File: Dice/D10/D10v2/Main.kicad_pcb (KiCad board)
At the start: 2 copper layers, 88.8 x 48.5 mm, 65 parts, among them J1 Conn_01x14, J2 Conn_01x04, J3 Conn_01x02, J4 DNP, P5 COILA, P6 COILB, U1 N52810_QFN32, U2 KXTJ3-1057, U3 PJ75AL50SA, U4 ME6215, U5 MCP73832T-2ACI/OT, U6 MT9700, U7 SN74LVC1G08, U8 TMR1366, Y1 32MHz 40ppm

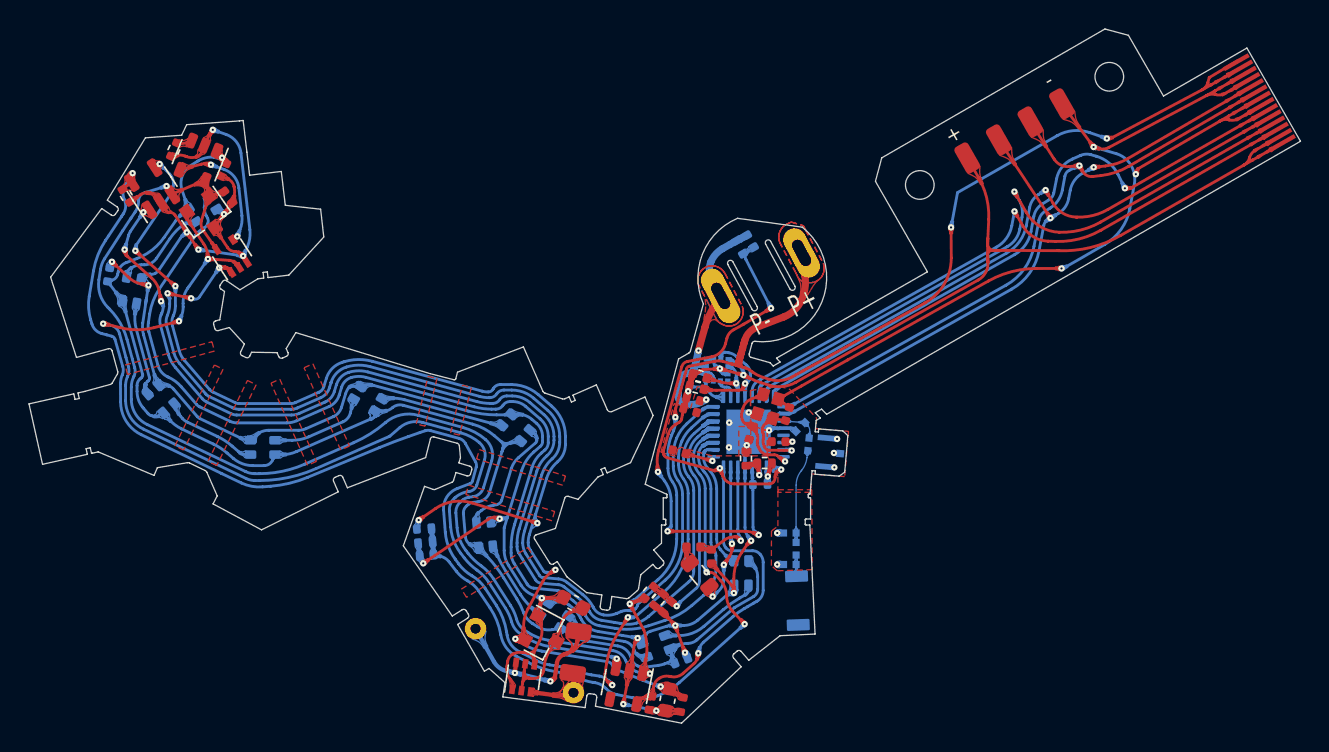
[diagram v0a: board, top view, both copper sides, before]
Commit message: Updated D6, D8, D10 boards
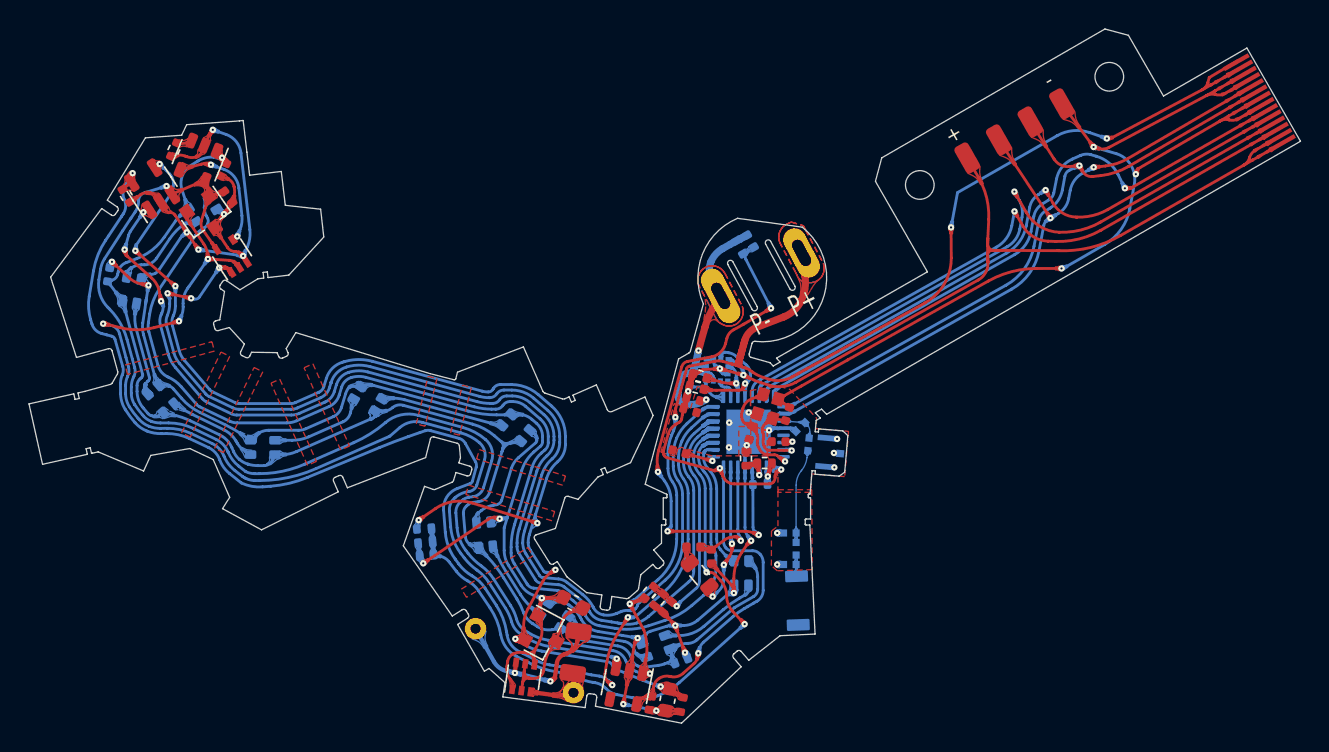
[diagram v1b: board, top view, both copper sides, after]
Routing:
- added copper zone on B.Cu, net Net-(D8-Pad3)
- added copper zone on B.Cu, net VDC
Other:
- outline, holes or cut-outs redrawn

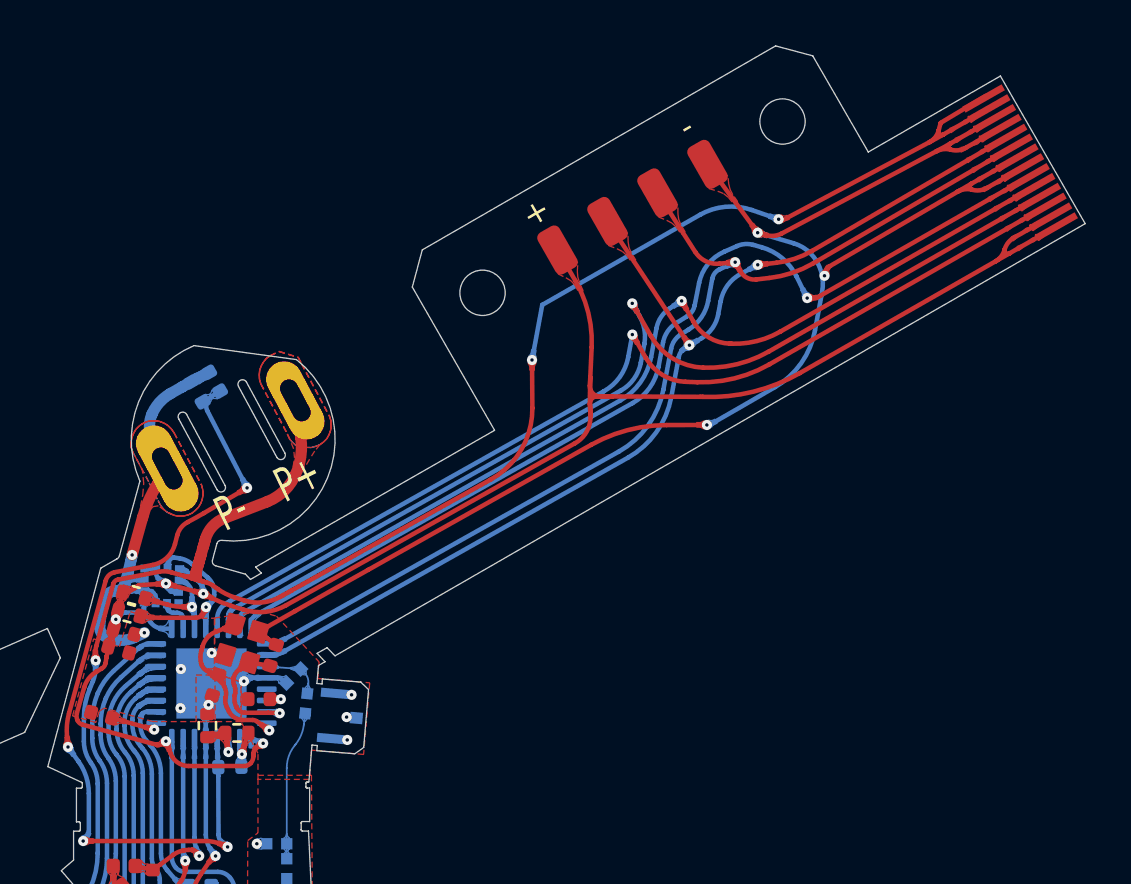
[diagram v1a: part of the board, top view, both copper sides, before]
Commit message: Updated all dice boards with smaller programming connector. Added ChargerV16
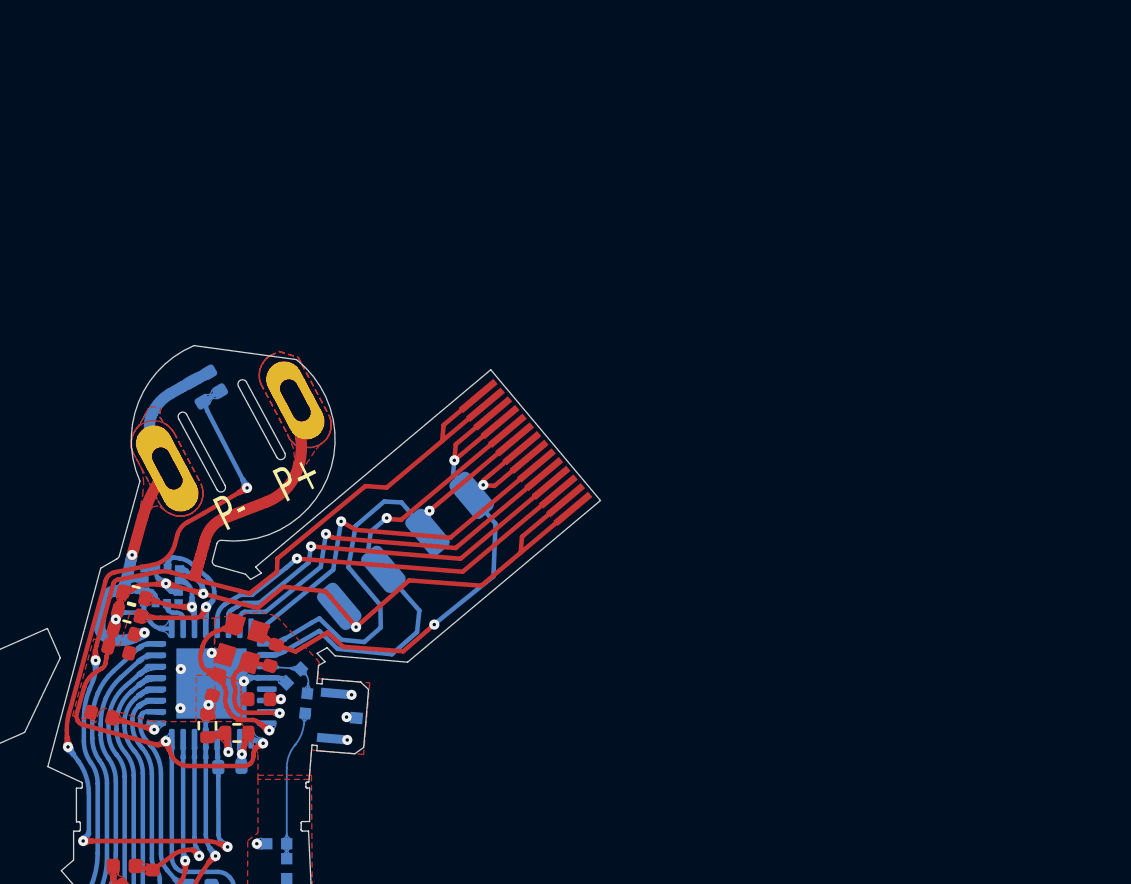
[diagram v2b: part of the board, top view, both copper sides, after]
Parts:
- J2: moved to B.Cu
- moved J1 25.9 mm to (162.8, 98.1), turned to -50 degrees
- moved J2 18.2 mm to (159.6, 105.0), turned to 40 degrees
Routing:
- net GND: track 258.1 -> 218.9 mm
- net VDD: track 107.6 -> 75.3 mm, vias 6 -> 7
- net +BATT: track 170.9 -> 140.9 mm, vias 6 -> 4
- net SWO: track 46.1 -> 17.5 mm
- net SWDIO: track 48.1 -> 20.7 mm, vias 2 -> 1
- net RESET: track 43.9 -> 16.6 mm
- net TXO: track 44.4 -> 17.9 mm
- net RXI: track 43.4 -> 17.2 mm
- net SWDCLK: track 47.1 -> 21.0 mm
- added copper zone on B.Cu, net Net-(C2-Pad2)
- added copper zone on B.Cu, net Net-(C3-Pad1)
- removed copper zone on F.Cu, net SWDCLK
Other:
- board size 88.8 x 48.5 mm -> 67.4 x 42.1 mm

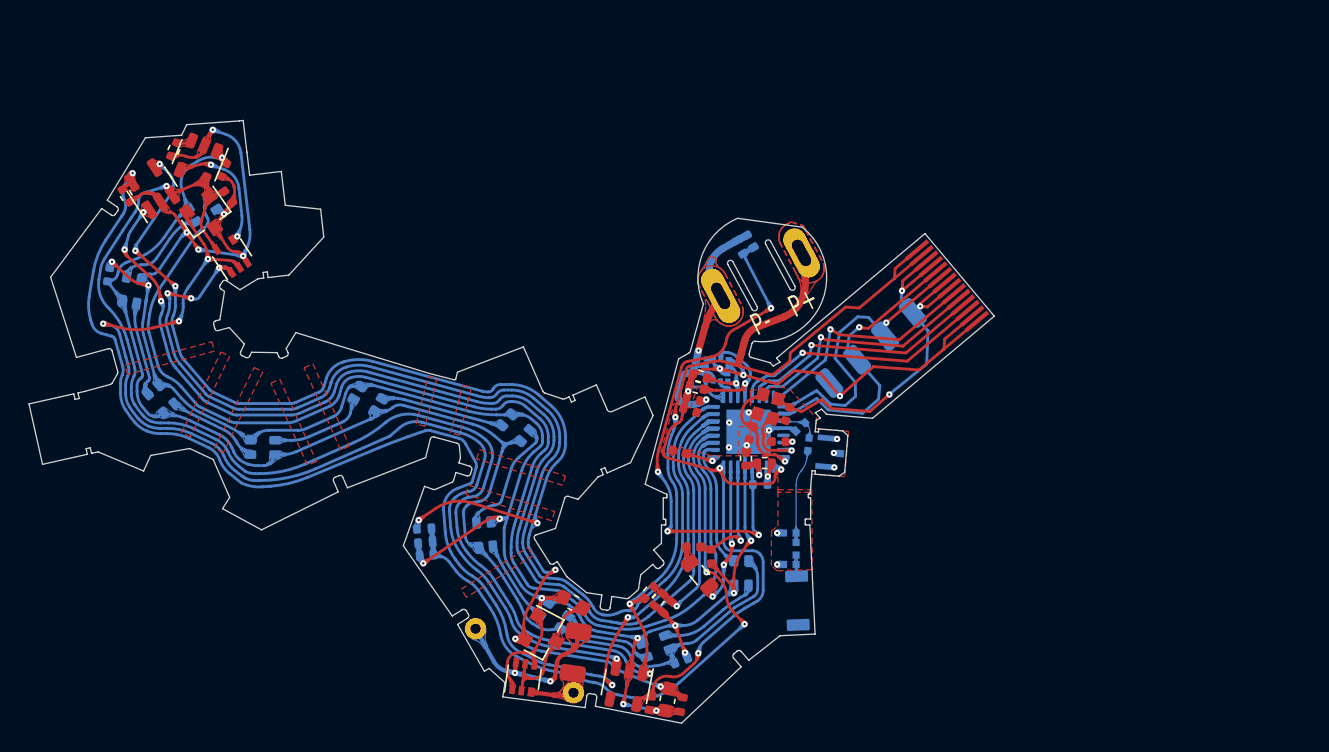
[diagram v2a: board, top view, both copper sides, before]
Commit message: Regenerate Gerbers for remaining dice
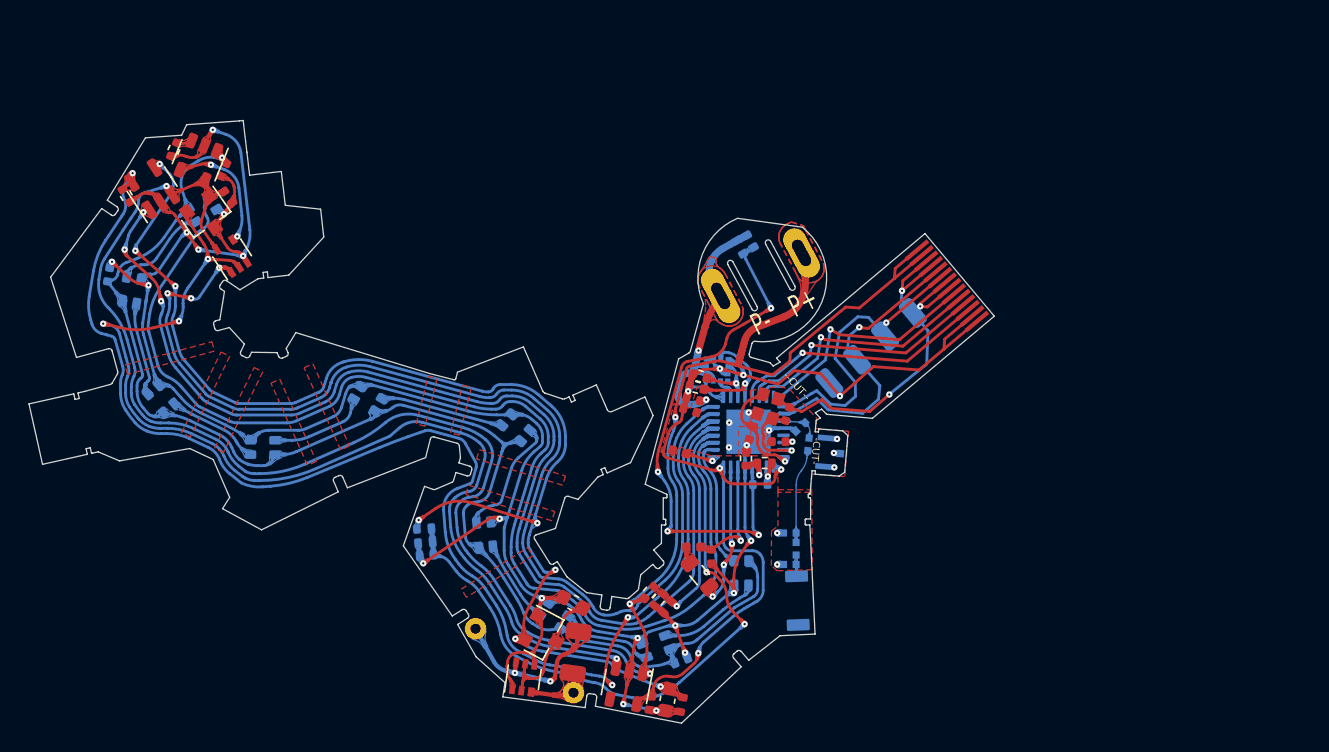
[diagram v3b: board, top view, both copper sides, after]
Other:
- outline, holes or cut-outs redrawn
- board text added: "-CUT-"
